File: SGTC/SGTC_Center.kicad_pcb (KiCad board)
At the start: 2 copper layers, 264.1 x 101.6 mm, 35 parts, among them J1 Conn_01x01_Pin, J10 Conn_01x04_Pin, J2 Conn_01x01_Pin, J3 Conn_01x01_Pin, J4 Conn_01x01_Pin, J5 Conn_01x01_Pin, J6 Conn_01x01_Pin, J7 Conn_01x01_Pin, J8 Conn_01x03_Pin, J9 Conn_01x04_Pin, U1 ADS131M03QPWRQ1, U2 TMP235A4DBZR

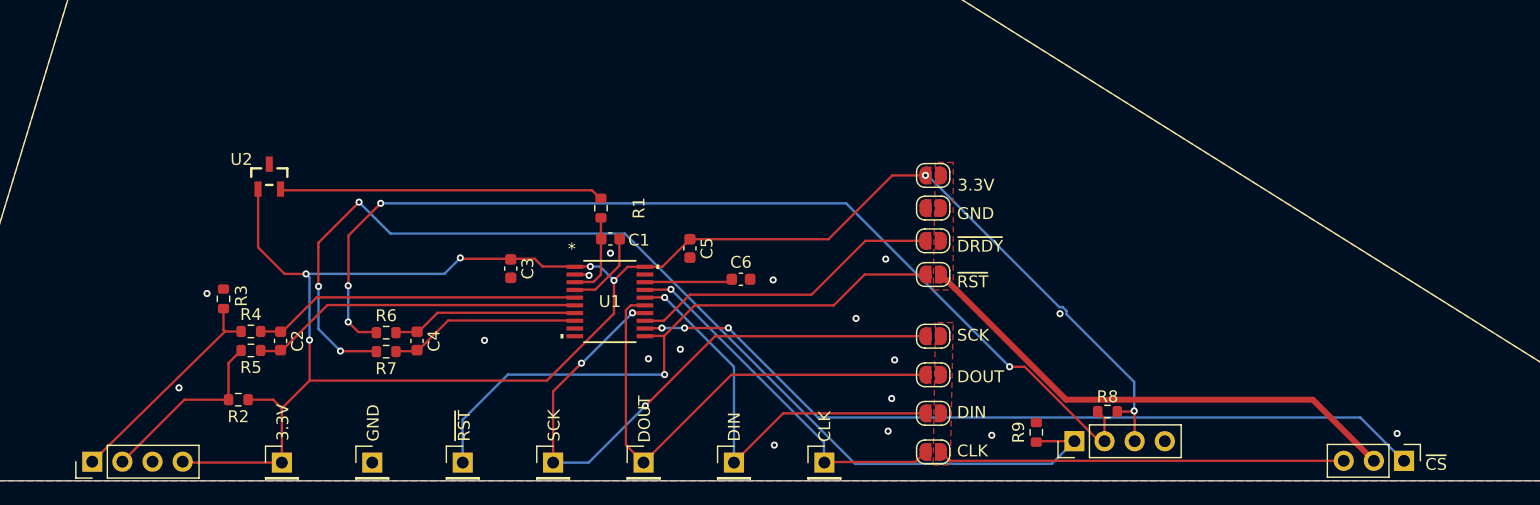
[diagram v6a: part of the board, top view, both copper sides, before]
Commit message: remake boards better with four layers
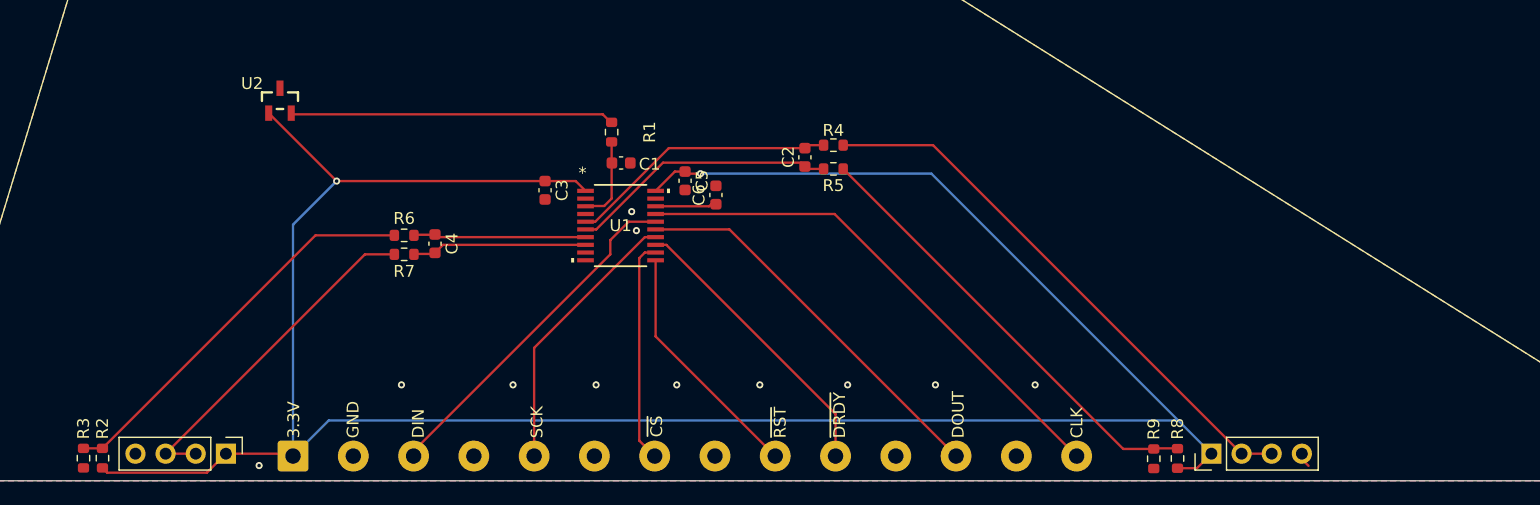
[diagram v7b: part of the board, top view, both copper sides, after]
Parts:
- removed J2, J3, J4, J5, J6, J7: Conn_01x01_Pin, Connector_PinHeader_2.54mm:PinHeader_1x01_P2.54mm_Vertical
- removed J8: Conn_01x03_Pin, Connector_PinHeader_2.54mm:PinHeader_1x03_P2.54mm_Vertical
- removed JP1, JP2, JP3, JP4, JP5, JP6, JP7, JP8: SolderJumper_2_Open, Jumper:SolderJumper-2_P1.3mm_Open_RoundedPad1.0x1.5mm
- C2, C4: value 5 nF -> 10 nF
- J1: value Conn_01x01_Pin -> Conn_01x14_Pin; footprint Connector_PinHeader_2.54mm:PinHeader_1x01_P2.54mm_Vertical -> TerminalBlock_Phoenix:TerminalBlock_Phoenix_MKDS-1,5-14-5.08_1x14_P5.08mm_Horizontal
- R4, R5, R6, R7: value 5 k -> 2.5 k
- moved R4 51.5 mm to (133.4, 111.8), turned to 180 degrees
- moved R5 51.4 mm to (133.4, 113.8), turned to 0 degrees
- moved C2 46.8 mm to (131.0, 112.8)
- moved J1 44.8 mm to (87.9, 138.0)
- moved R3 17.9 mm to (70.2, 138.2)
- moved R2 12.5 mm to (71.8, 138.2), turned to -90 degrees
- moved J10 11.6 mm to (165.3, 137.8)
- moved J9 11.3 mm to (82.2, 137.8), turned to -90 degrees
- moved R9 10.1 mm to (160.4, 138.2), turned to 90 degrees
- moved C4 8.34 mm to (99.8, 120.1)
- moved R6 8.34 mm to (97.2, 119.4)
- moved R7 8.34 mm to (97.2, 121.0)
- moved C6 7.41 mm to (123.5, 116.0), turned to 90 degrees
- moved C3 7.21 mm to (109.1, 115.6)
- moved R8 7.10 mm to (162.4, 138.2), turned to 90 degrees
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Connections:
- J1 pad 1: ADCCLK -> +3.3V
- J10 pad 1: GAUGE2_IN_N -> +3.3V
- J10 pad 3: +3.3V -> GAUGE2_IN_P
- J9 pad 1: GAUGE1_IN_N -> +3.3V
- J9 pad 3: GND -> GAUGE1_IN_P
- J9 pad 4: +3.3V -> GND
- R2 pad 1: +3.3V -> GAUGE1_IN_N
- R2 pad 2: GAUGE1_IN_P -> +3.3V
- R3 pad 1: GND -> GAUGE1_IN_N
- R3 pad 2: GAUGE1_IN_N -> GND
- R4 pad 1: GAUGE1_IN_N -> GAUGE2_IN_P
- R5 pad 2: GAUGE1_IN_P -> GAUGE2_IN_N
- R6 pad 1: GAUGE2_IN_P -> GAUGE1_IN_N
- R7 pad 2: GAUGE2_IN_N -> GAUGE1_IN_P
- R8 pad 2: GAUGE2_IN_P -> GAUGE2_IN_N
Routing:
- net +3.3V: track 149.3 -> 209.1 mm, vias 7 -> 2
- net GAUGE2_IN_N: track 91.3 -> 38.0 mm, vias 3 -> 0
- net ~{CS}: track 68.7 -> 18.8 mm, vias 3 -> 0
- net Net-(J8-Pin_2): track 43.0 -> 0.00 mm
- net GAUGE2_IN_P: track 86.0 -> 46.9 mm, vias 4 -> 0
- net Net-(J8-Pin_3): track 34.3 -> 0.00 mm
- net ~{SYNC}/~{RST}: track 51.3 -> 20.7 mm, vias 1 -> 0
- net GAUGE1_IN_N: track 3.34 -> 33.6 mm
- net SPICLK: track 52.3 -> 23.2 mm, vias 3 -> 0
- net GAUGE1_IN_P: track 15.7 -> 28.8 mm
- net ADCCLK: track 31.0 -> 43.9 mm, vias 1 -> 0
- net DOUT: track 42.1 -> 33.2 mm
- net GND: track 8.24 -> 0.60 mm, vias 17 -> 11
- net DIN: track 35.9 -> 29.5 mm, vias 1 -> 0
- net Net-(U1-AIN1P): track 28.1 -> 22.6 mm
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- added copper zone on In2.Cu, net GND
- removed copper zone on F.Cu, net Net-(J8-Pin_2)
- removed copper zone on F.Cu, net Net-(J8-Pin_3)
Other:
- copper layers 2 -> 4
